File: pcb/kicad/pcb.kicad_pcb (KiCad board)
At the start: 2 copper layers, 320.5 x 103.9 mm, 93 parts, among them K00 KEYSW, K01 KEYSW, K02 KEYSW, K03 KEYSW, K04 KEYSW, K05 KEYSW, K10 KEYSW, K11 KEYSW, K12 KEYSW, K13 KEYSW, K14 KEYSW, K15 KEYSW, K20 KEYSW, K21 KEYSW, K22 KEYSW, K23 KEYSW, K24 KEYSW, K25 KEYSW, K33 KEYSW, K34 KEYSW, K35 KEYSW, K40 KEYSW, K41 KEYSW, K42 KEYSW, K43 KEYSW, K44 KEYSW, K45 KEYSW, K50 KEYSW, K51 KEYSW, K52 KEYSW, K53 KEYSW, K54 KEYSW, K55 KEYSW, K60 KEYSW, K61 KEYSW, K62 KEYSW, K63 KEYSW, K64 KEYSW, K65 KEYSW, K70 KEYSW, K71 KEYSW, K72 KEYSW

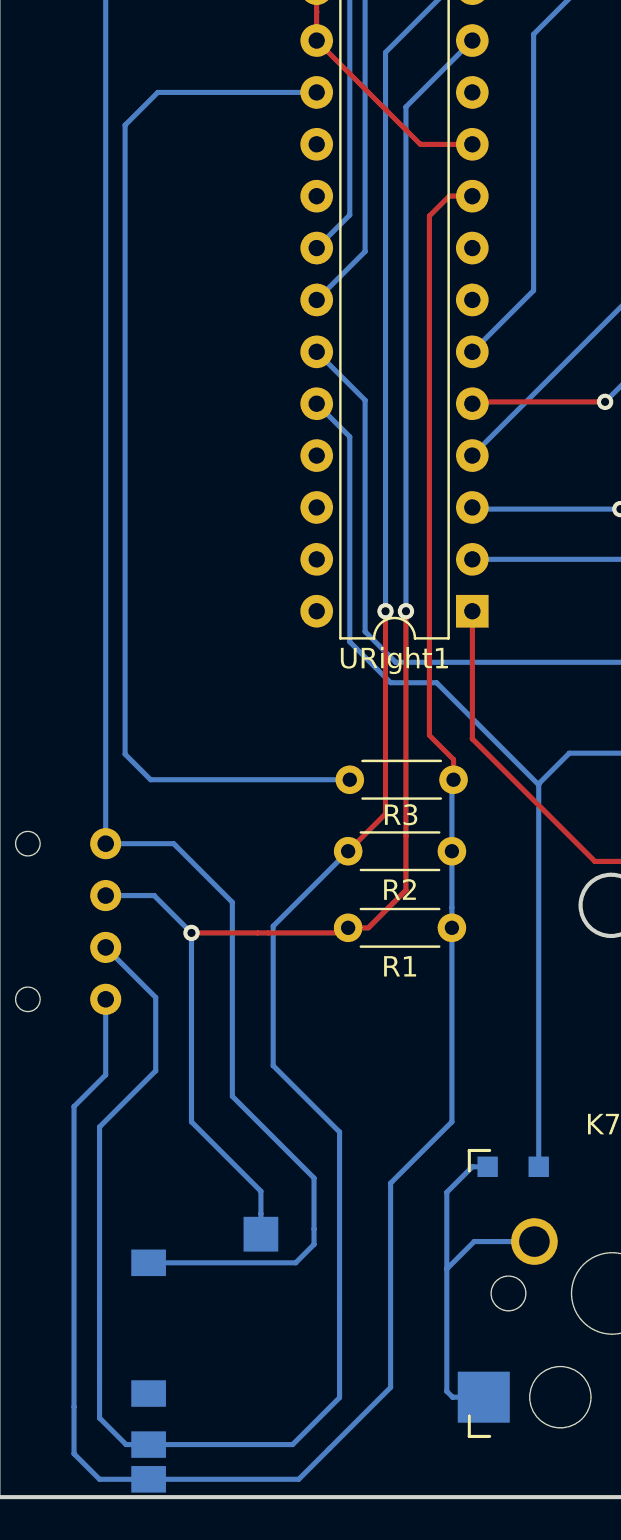
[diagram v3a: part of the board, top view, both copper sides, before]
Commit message: PCB: increase size of resistor footprints
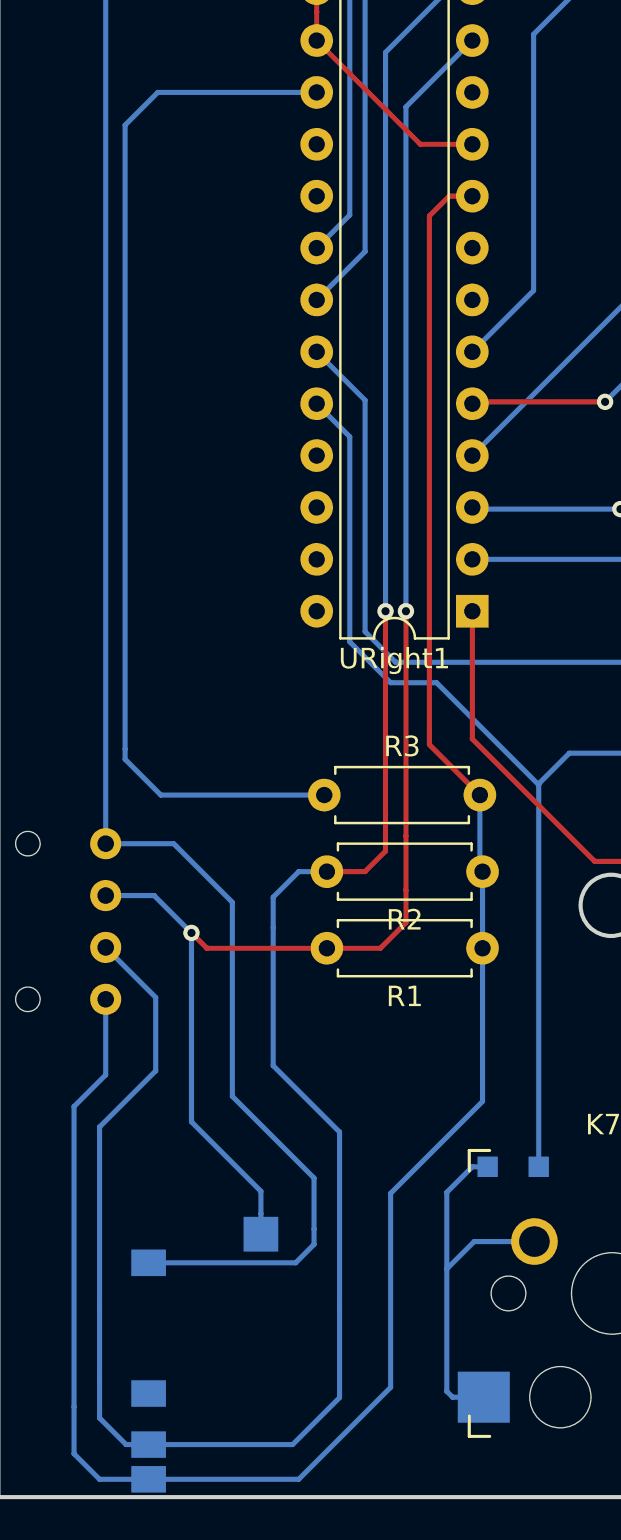
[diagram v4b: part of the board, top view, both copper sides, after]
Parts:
- R1, R2, R3: footprint Resistor_THT:R_Axial_DIN0204_L3.6mm_D1.6mm_P5.08mm_Horizontal -> Resistor_THT:R_Axial_DIN0207_L6.3mm_D2.5mm_P7.62mm_Horizontal
- moved R1 1.80 mm to (181.5, 105.2)
- moved R2 1.80 mm to (181.5, 101.5)
- moved R3 1.46 mm to (173.8, 97.8)
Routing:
- net SDAR: track 113.5 -> 115.4 mm
- net SCLR: track 75.4 -> 77.0 mm
- net +5vR: track 102.4 -> 103.6 mm
- net Net-(R3-Pad1): track 52.4 -> 51.6 mm

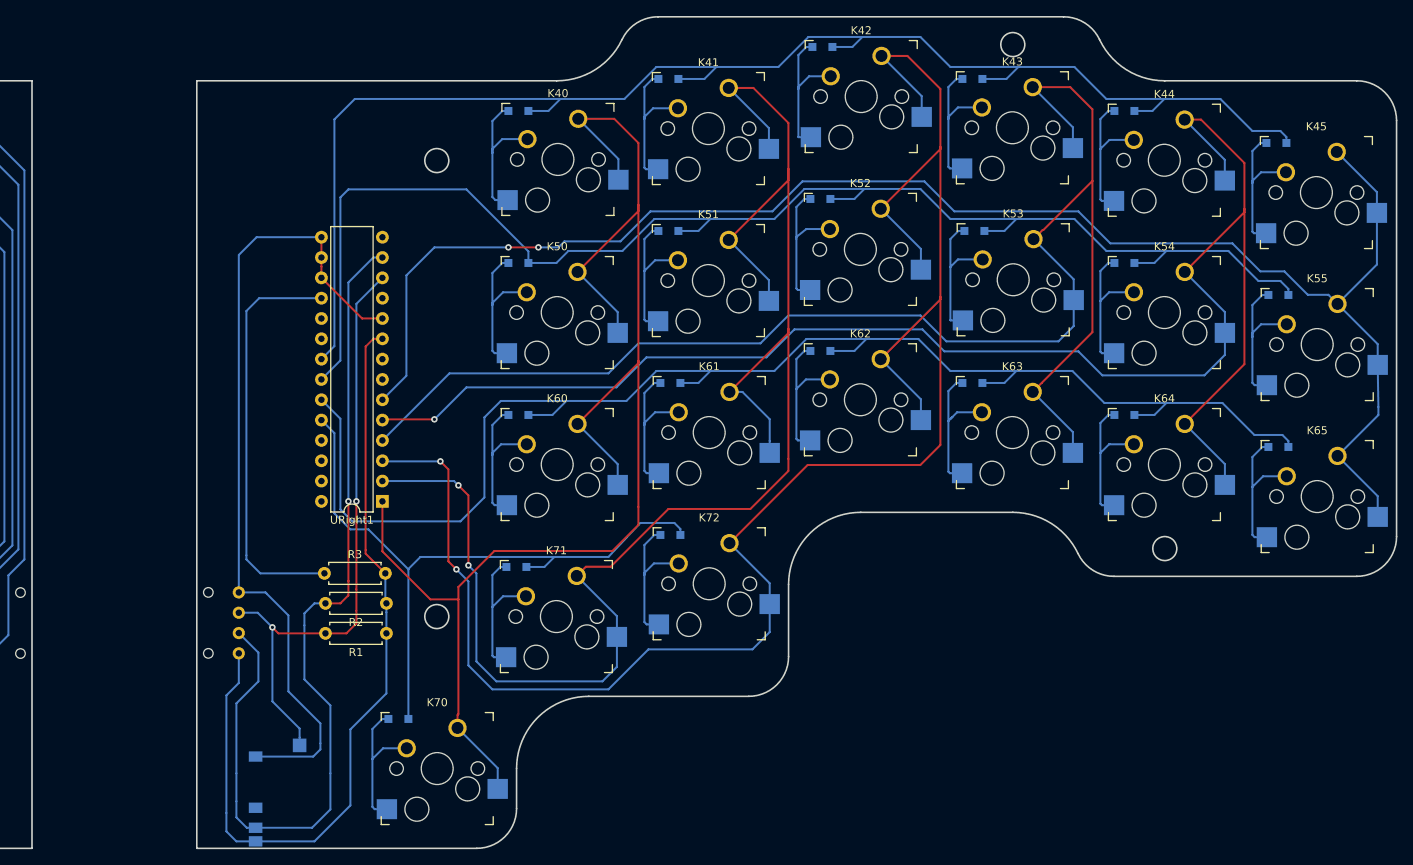
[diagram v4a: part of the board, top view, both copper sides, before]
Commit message: PCB: Fix position of female pin connector
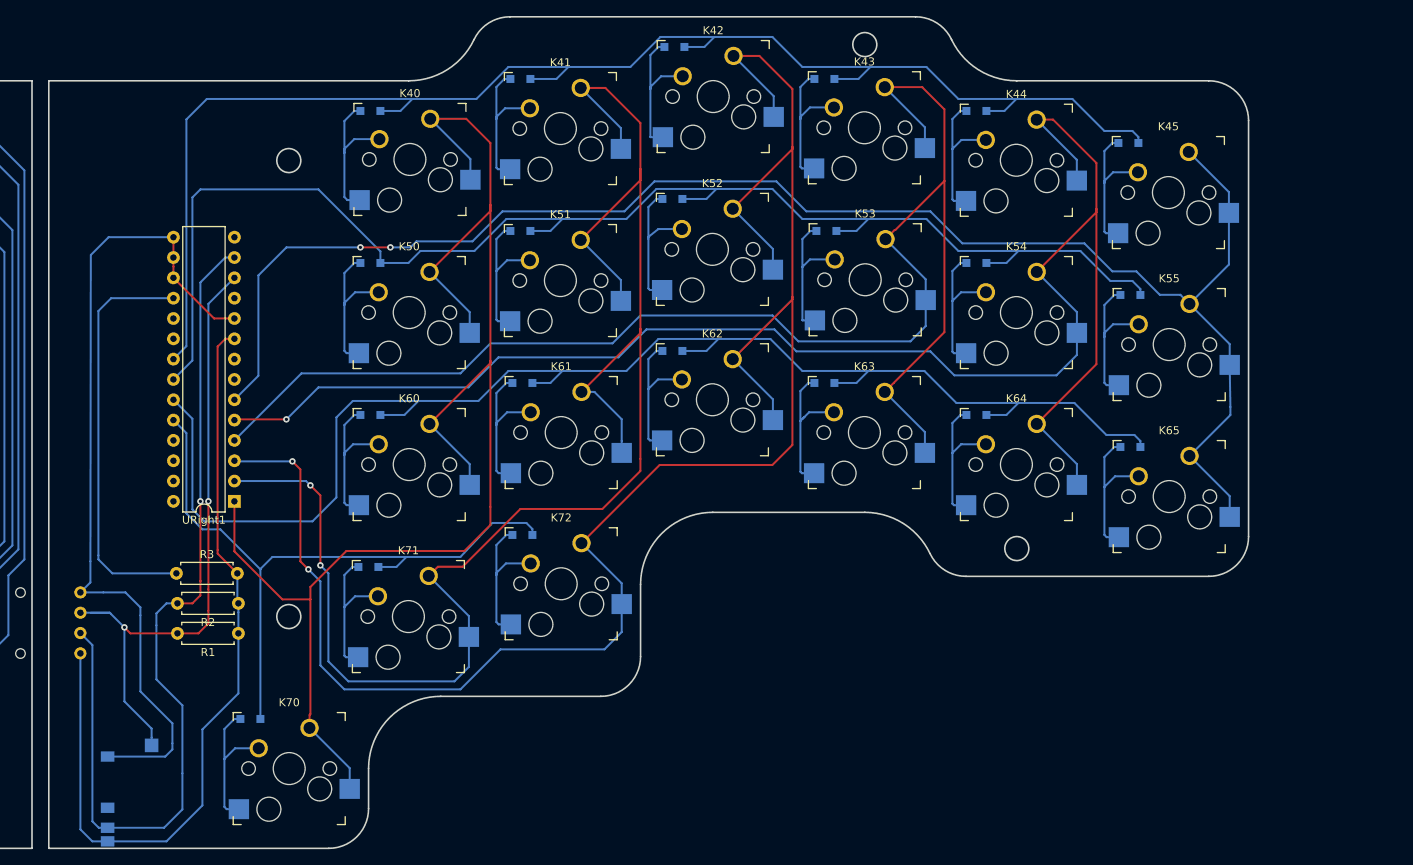
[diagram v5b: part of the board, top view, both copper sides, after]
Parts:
- JLeft2: footprint 42_keyboard:Conn-1x4 -> 42_keyboard:Conn-1x4-Male
- JRight2: footprint 42_keyboard:Conn-1x4 -> 42_keyboard:Conn-1x4-Female
- moved JRight2 19.8 mm to (143.2, 107.8)
- moved K53 18.5 mm to (241.3, 61.0)
- moved D40 18.5 mm to (179.5, 40.0)
- moved D41 18.5 mm to (198.2, 36.0)
- moved D42 18.5 mm to (217.5, 31.9)
- moved D43 18.5 mm to (236.2, 36.0)
- moved D44 18.5 mm to (255.2, 40.0)
- moved D45 18.5 mm to (274.2, 44.0)
- moved D50 18.5 mm to (179.5, 59.0)
- moved D51 18.5 mm to (198.2, 55.0)
- moved D52 18.5 mm to (217.2, 51.0)
- moved D53 18.5 mm to (236.5, 55.0)
- moved D54 18.5 mm to (255.2, 59.0)
- moved D55 18.5 mm to (274.5, 63.0)
- moved D60 18.5 mm to (179.5, 78.0)
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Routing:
- net SCLR: track 77.0 -> 80.7 mm
- net GNDR: track 102.5 -> 104.9 mm
- net SDAR: track 115.4 -> 113.6 mm
- net +5vR: track 103.6 -> 102.5 mm
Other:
- board size 320.5 x 103.9 mm -> 302 x 103.9 mm
